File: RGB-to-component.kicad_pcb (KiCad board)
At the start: 2 copper layers, 50 x 70 mm, 55 parts, among them J1 VGA, J3 USB_C_Receptacle_Power, J4 SCART_CONN, J5 3xRCA_CONN, U1 SC6206B-65K5, U2 TPF144-VR, U3 RS8752XQ, U4 TPF-141TR, U6 74AHC1G86, U7 74AHC1G86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

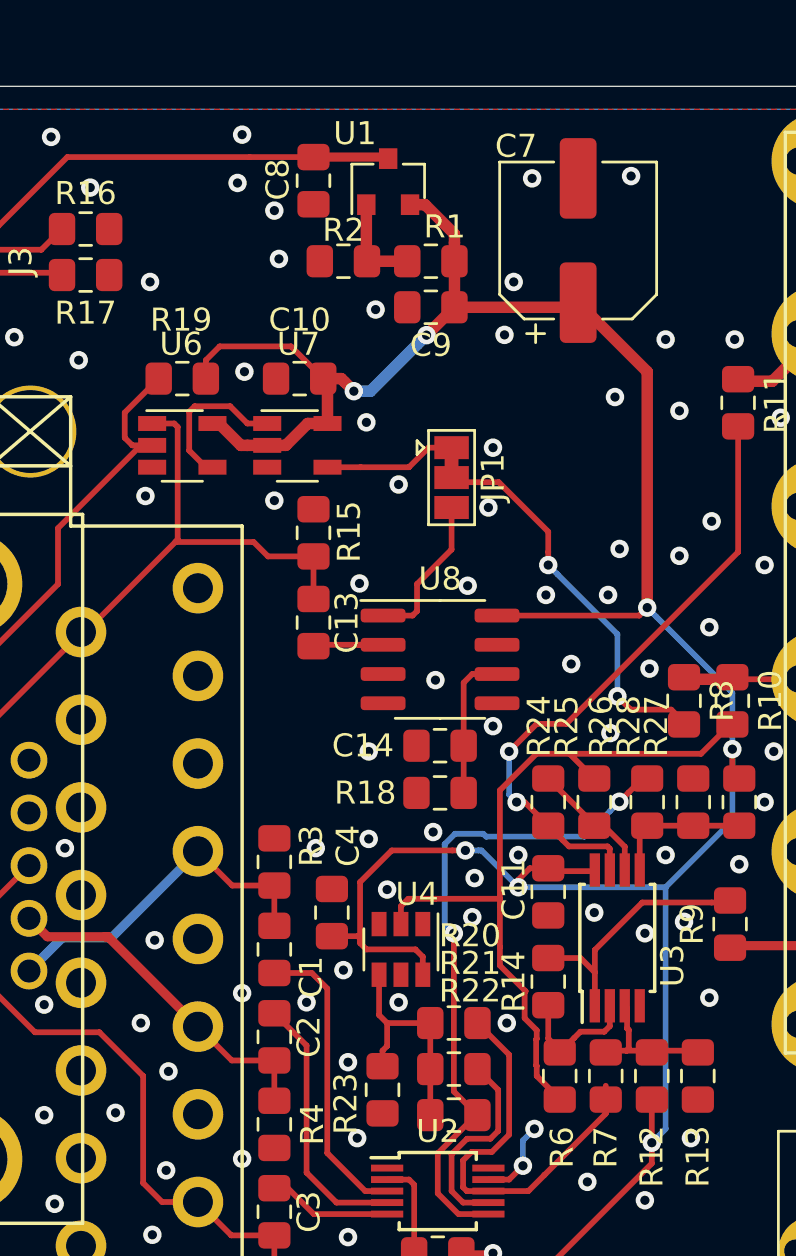
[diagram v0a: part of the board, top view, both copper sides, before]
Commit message: reusing video amp, ferrite, power led, updated jlc files
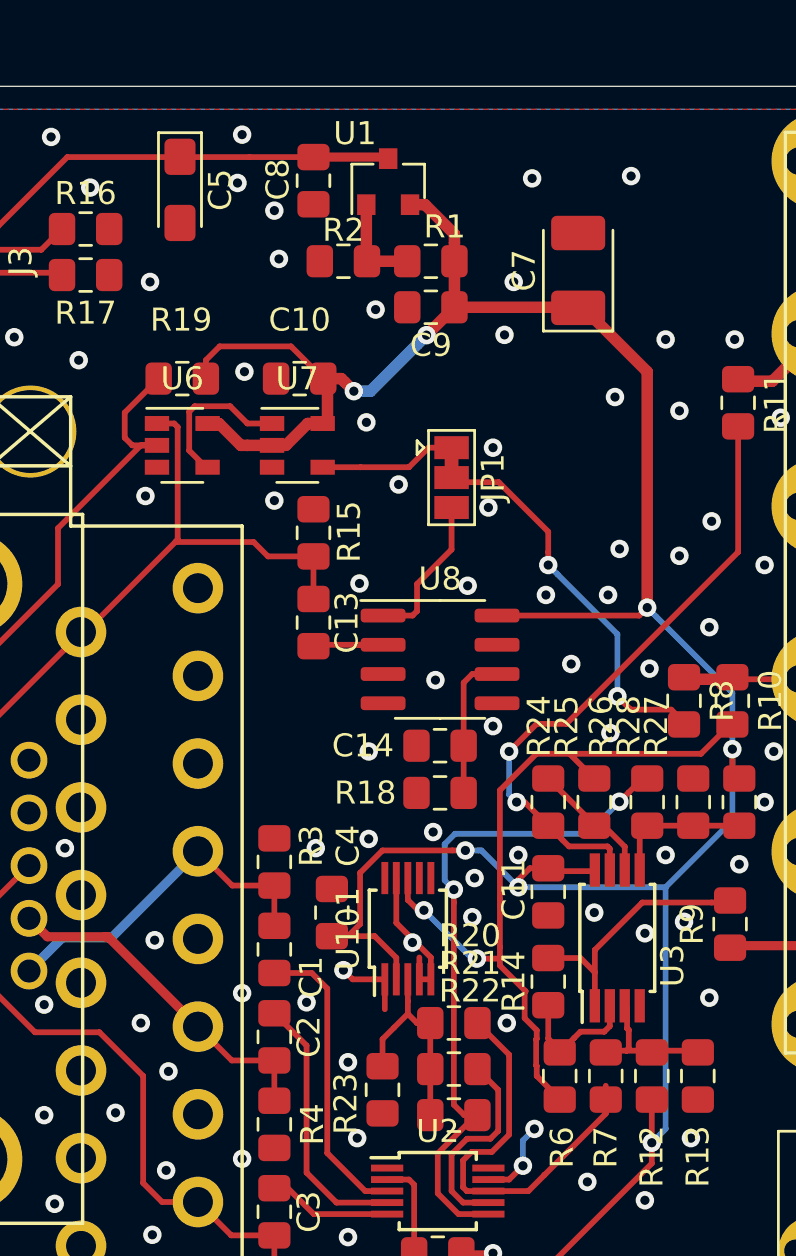
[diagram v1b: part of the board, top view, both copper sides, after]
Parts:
- removed U4: TPF-141TR, Package_TO_SOT_SMD:SOT-23-6
- added C5: 10u, Capacitor_Tantalum_SMD:CP_EIA-3216-18_Kemet-A_Pad1.58x1.35mm_HandSolder, F.Cu at (33.7, 44.5)
- added U101: TPF144-VR, Package_SO:MSOP-10_3x3mm_P0.5mm, F.Cu at (43.6, 76.6)
- C7: value 33u -> 100u; footprint Capacitor_SMD:CP_Elec_6.3x7.7 -> Capacitor_Tantalum_SMD:CP_EIA-3528-21_Kemet-B_Pad1.50x2.35mm_HandSolder
- R20: value 1070 -> 1k
- R21: value 549 -> 511
- R22: value 2940 -> 2740
- R23: value 323 -> 300
- U6, U7: footprint Package_TO_SOT_SMD:TSOT-23-5 -> Package_TO_SOT_SMD:SOT-23-5
- moved C7 1.30 mm to (51.0, 48.0)
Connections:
- U2 pad 1: Net-(U2-Pad1) -> GND
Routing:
- net GND: track 4.93 -> 14.7 mm, vias 104 -> 103
- net /2Y: track 32.6 -> 33.4 mm, vias 0 -> 2
- net Net-(R20-Pad1): track 10.1 -> 9.37 mm

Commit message: starting panelise
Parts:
- added D101: LED, LED_SMD:LED_0805_2012Metric, F.Cu at (58.0, 46.9)
- added GOTE2: Fiducial, videobits:borgar, B.Cu at (47.8, 80.7)
- added L101: 10u, Inductor_SMD:L_0805_2012Metric_Pad1.15x1.40mm_HandSolder, F.Cu at (30.6, 43.1)
- added R101: 1k, Resistor_SMD:R_0805_2012Metric_Pad1.15x1.40mm_HandSolder, F.Cu at (54.8, 49.6)
- moved R6 23.9 mm to (56.6, 60.0), turned to 270 degrees
- moved R13 23.7 mm to (50.6, 60.0), turned to 270 degrees
- moved R7 23.1 mm to (54.6, 60.0), turned to 270 degrees
- moved R12 23.1 mm to (52.6, 60.0), turned to 270 degrees
- moved R9 22.4 mm to (57.9, 54.0), turned to 270 degrees
- moved R14 16.5 mm to (57.1, 64.2)
- moved R11 15.9 mm to (59.0, 69.6)
- moved R10 12.3 mm to (56.9, 79.0), turned to 90 degrees
- moved R8 12.3 mm to (54.9, 79.0), turned to 90 degrees
- moved U3 11.1 mm to (54.1, 66.0), turned to 270 degrees
- moved C11 10.2 mm to (57.1, 68.0), turned to 90 degrees
- moved R27 9.23 mm to (48.8, 71.9), turned to 90 degrees
- moved R24 7.44 mm to (57.1, 71.9), turned to 90 degrees
- moved R28 5.26 mm to (50.8, 71.9), turned to 90 degrees
- moved R25 3.49 mm to (55.1, 71.9), turned to 90 degrees
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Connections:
- J3 pad A9: +5V -> Net-(J3-PadA9)
- J3 pad B9: +5V -> Net-(J3-PadA9)
- R10 pad 1: Net-(J5-Pad1) -> Net-(J5-Pad3)
- R11 pad 1: Net-(J5-Pad2) -> Net-(J5-Pad1)
- R8 pad 1: Net-(J5-Pad1) -> Net-(J5-Pad3)
- R9 pad 1: Net-(J5-Pad3) -> Net-(J5-Pad2)
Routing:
- net /2R: track 17.9 -> 43.8 mm, vias 0 -> 2
- net /2Pb: track 27.3 -> 6.31 mm, vias 2 -> 0
- net /SYNC: track 16.9 -> 32.9 mm
- net VCC: track 128.7 -> 112.6 mm, vias 7 -> 2
- net +5V: track 24.1 -> 11.2 mm
- net Net-(J3-PadA9): track 0.00 -> 10.9 mm
- net /2Y: track 33.4 -> 41.5 mm, vias 2 -> 0
- net Net-(R14-Pad1): track 5.69 -> 10.4 mm
- net GND: track 14.7 -> 10.7 mm, vias 103 -> 105
- net Net-(J5-Pad3): track 11.4 -> 14.4 mm
- net Net-(D101-Pad2): track 0.00 -> 2.91 mm
- net /2B: track 29.6 -> 26.8 mm
- net Net-(J5-Pad1): track 13.4 -> 12.2 mm, vias 0 -> 1
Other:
- net class Default: clearance 0.2 -> 0.15; trace_width 0.25 -> 0.15
- rule trace_clearance: 0.2 -> 0.15
- rule trace_min: 0.2 -> 0.15
- board text added: "RGB to YPbPr 2020-06-12 rev 2.3 wakabavideo.com"
- board text removed: "RGB to YPbPr 2020-03-16 rev 2.2 wakabavideo.com"

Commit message: fixed resistor
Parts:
- U3: footprint Package_SO:TSSOP-8_4.4x3mm_P0.65mm -> Package_SO:MSOP-8_3x3mm_P0.65mm
- moved U3 0.51 mm to (54.0, 66.5)
- moved JR1 0.10 mm to (69.6, 90.6)
- moved JU1 0.10 mm to (69.6, 103.6)
- moved C10 0.10 mm to (38.8, 52.7)
- moved C11 0.10 mm to (57.0, 68.0)
- moved C12 0.10 mm to (44.8, 90.7)
- moved C13 0.10 mm to (39.4, 63.3)
- moved C14 0.10 mm to (44.9, 68.7)
- moved C5 0.10 mm to (33.6, 44.5)
- moved C7 0.10 mm to (50.9, 48.0)
- moved C8 0.10 mm to (39.4, 44.1)
- moved C9 0.10 mm to (44.5, 49.6)
- moved D101 0.10 mm to (57.9, 46.9)
- moved GOTE1 0.10 mm to (53.9, 96.6)
- moved J1 0.10 mm to (24.5, 75.0)
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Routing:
- net Net-(R12-Pad2): track 6.78 -> 8.40 mm
- net /2Pr: track 11.2 -> 12.4 mm
- net GND: vias 105 -> 104

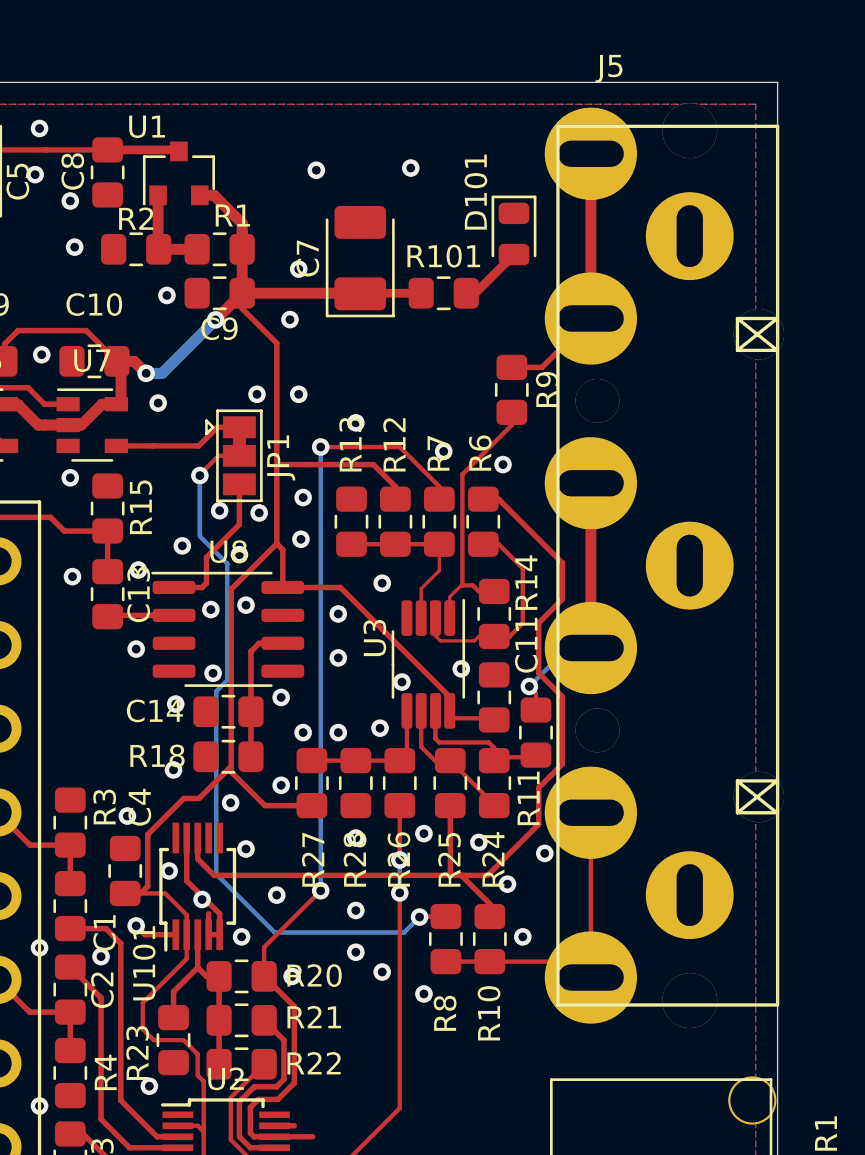
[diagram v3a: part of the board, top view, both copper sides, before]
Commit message: changed RCA jacks to single centre pin style, AHCT gates for VGA sync
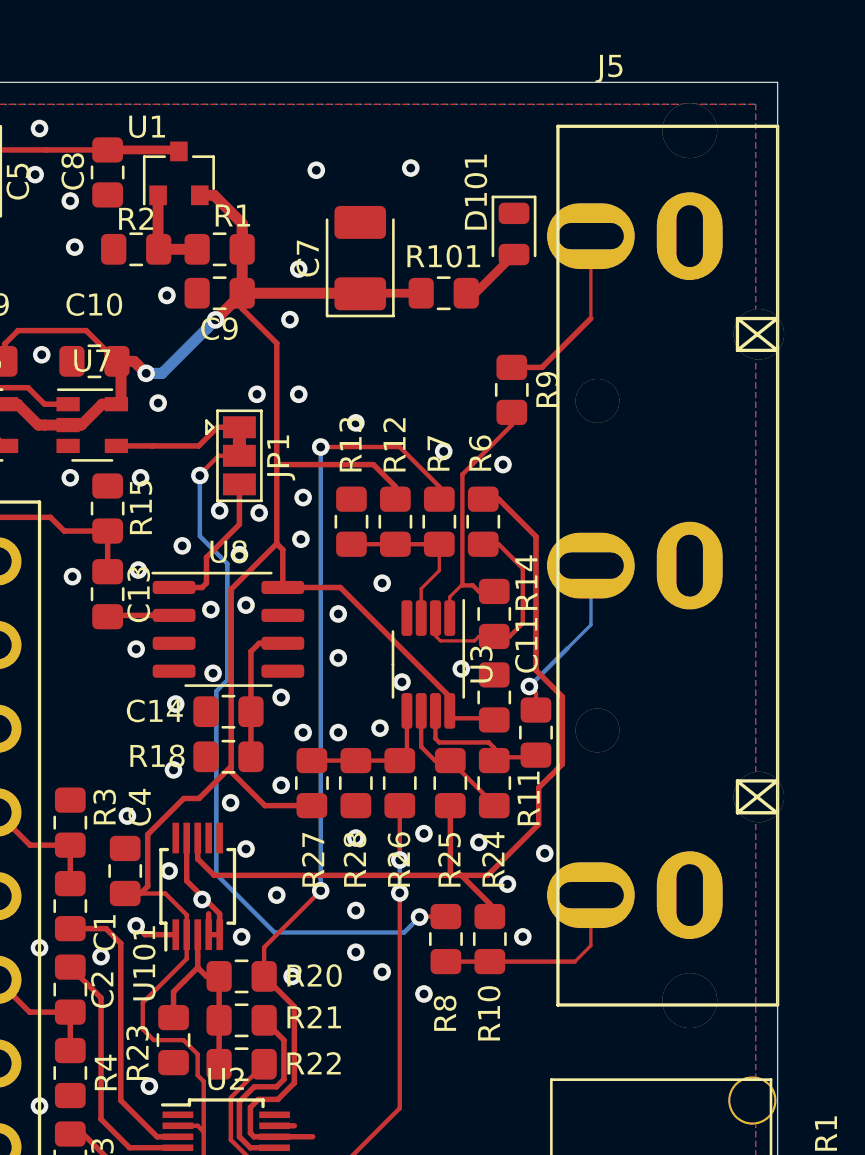
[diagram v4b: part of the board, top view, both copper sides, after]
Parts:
- J5: footprint custom_components:3xRCA_CONN -> videobits:3xRCA_CONN_SINGLE
- U3: value RS8752XQ -> RS8752XM
- U6, U7: value 74AHC1G86 -> 74AHCT1G86
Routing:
- net Net-(J5-Pad3): track 14.4 -> 9.20 mm
- net Net-(J5-Pad1): track 12.2 -> 7.86 mm
- net Net-(J5-Pad2): track 12.0 -> 8.27 mm
- net /2Y: track 41.5 -> 40.6 mm
- net GND: vias 104 -> 105

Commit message: swapped opamp for SOIC package
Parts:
- U3: value RS8752XM -> RS8752XK; footprint Package_SO:MSOP-8_3x3mm_P0.65mm -> Package_SO:SOIC-8_3.9x4.9mm_P1.27mm
- moved U3 1.17 mm to (53.0, 65.9)
- moved C12 0.20 mm to (44.8, 90.9)
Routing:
- net Net-(R24-Pad1): track 5.76 -> 7.65 mm
- net Net-(R14-Pad1): track 9.97 -> 11.2 mm
- net Net-(R12-Pad2): track 8.40 -> 7.16 mm
- net Net-(R26-Pad2): track 6.06 -> 7.20 mm
- net /2Pb: track 6.31 -> 7.42 mm
- net /2Pr: track 12.4 -> 11.4 mm
- net VCC: track 112.6 -> 113.3 mm
- net GND: vias 105 -> 99
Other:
- board text added: "RGB to YPbPr 2021-05-10 rev 2.4 wakabavideo.com"
- board text removed: "RGB to YPbPr 2020-06-12 rev 2.3 wakabavideo.com"

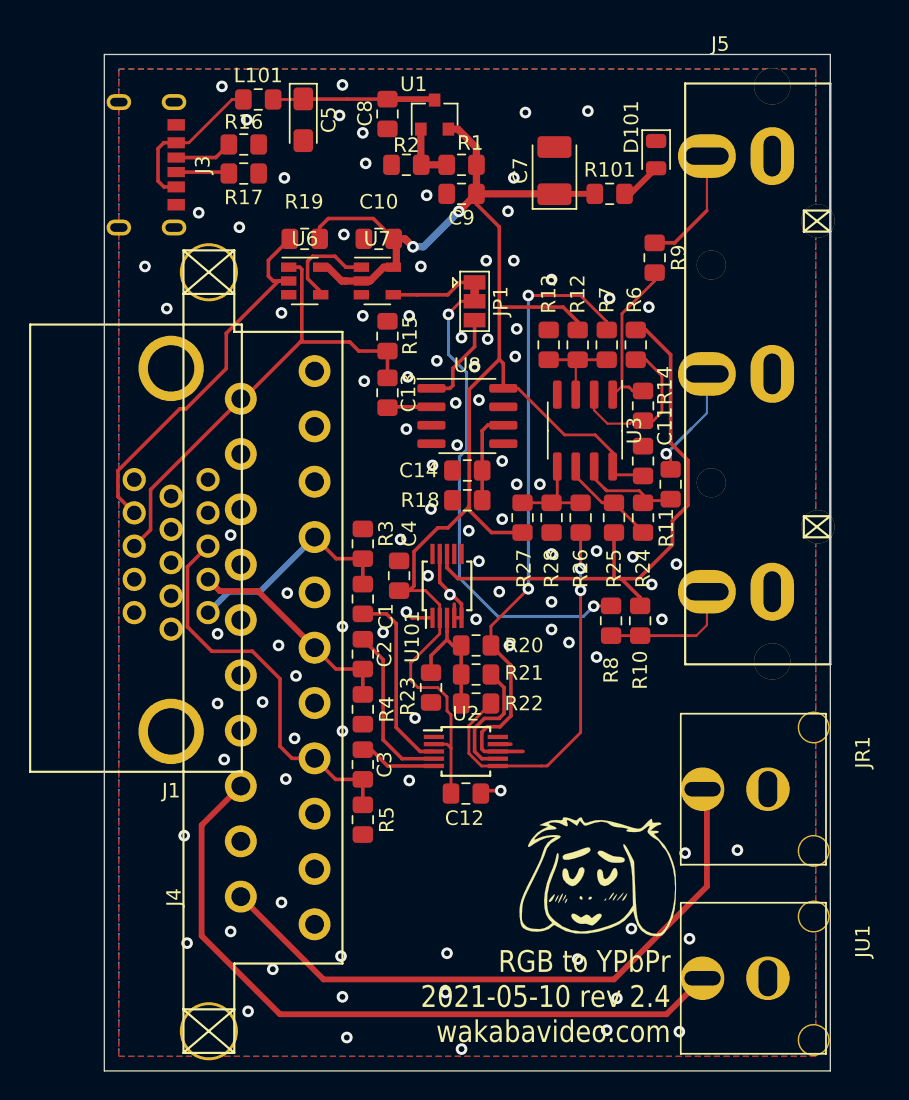
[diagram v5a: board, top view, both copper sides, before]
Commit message: converting to kicad 6
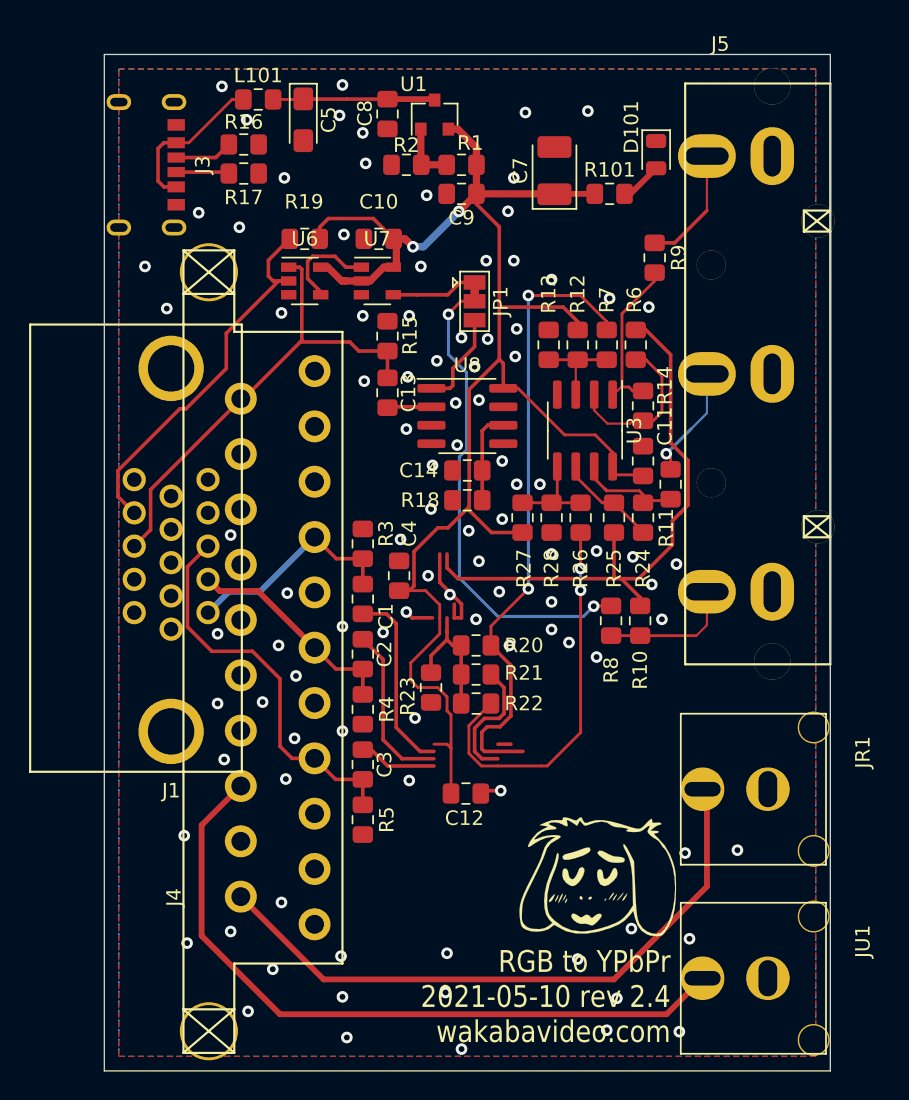
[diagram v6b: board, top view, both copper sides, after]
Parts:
- removed U101, U2: TPF144-VR, Package_SO:MSOP-10_3x3mm_P0.5mm
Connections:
- J1 pad 11: Net-(J1-Pad11) -> unconnected-(J1-Pad11)
- J1 pad 12: Net-(J1-Pad12) -> unconnected-(J1-Pad12)
- J1 pad 15: Net-(J1-Pad15) -> unconnected-(J1-Pad15)
- J1 pad 4: Net-(J1-Pad4) -> unconnected-(J1-Pad4)
- J1 pad 9: Net-(J1-Pad9) -> unconnected-(J1-Pad9)
- J4 pad 1: Net-(J4-Pad1) -> unconnected-(J4-Pad1)
- J4 pad 10: Net-(J4-Pad10) -> unconnected-(J4-Pad10)
- J4 pad 12: Net-(J4-Pad12) -> unconnected-(J4-Pad12)
- J4 pad 16: Net-(J4-Pad16) -> unconnected-(J4-Pad16)
- J4 pad 19: Net-(J4-Pad19) -> unconnected-(J4-Pad19)
- J4 pad 3: Net-(J4-Pad3) -> unconnected-(J4-Pad3)
- U8 pad 3: Net-(U8-Pad3) -> unconnected-(U8-Pad3)
- U8 pad 5: Net-(U8-Pad5) -> unconnected-(U8-Pad5)
- U8 pad 7: Net-(U8-Pad7) -> unconnected-(U8-Pad7)
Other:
- net class Default removed
